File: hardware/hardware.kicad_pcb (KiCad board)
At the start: 2 copper layers, 19 parts, among them J1 Conn_01x02, J2 Conn_01x02, P1 USB_C_Plug, U2 ATmega328PB-A, U3 LM1117S-5, U4 CH340C, Y1 Crystal_GND24

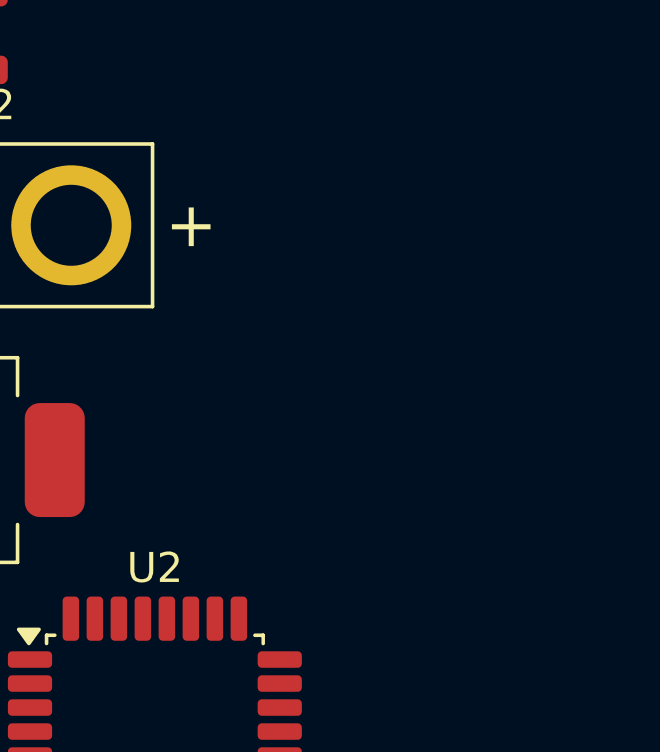
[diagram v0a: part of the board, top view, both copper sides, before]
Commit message: add isp connector
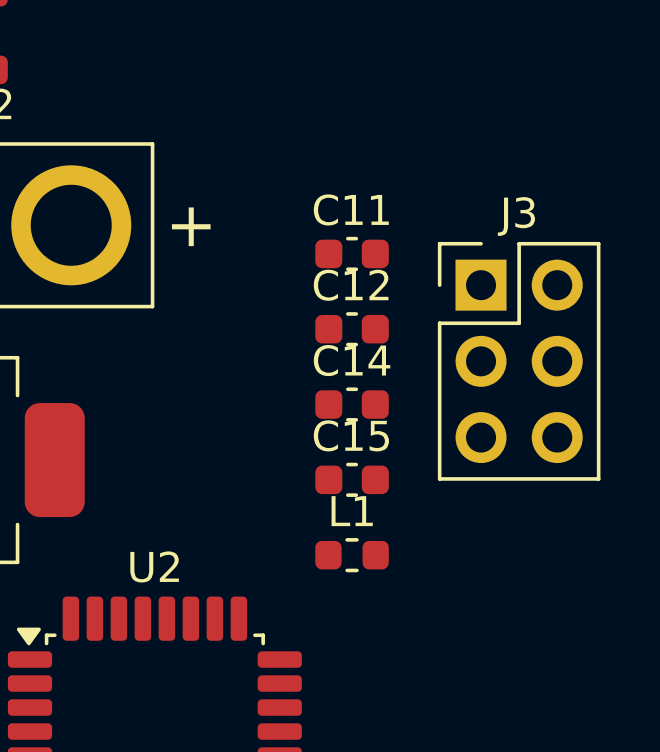
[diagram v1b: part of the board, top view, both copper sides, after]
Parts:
- added C11: 100n, Capacitor_SMD:C_0603_1608Metric, F.Cu at (134.9, 85.9)
- added C12: 100n, Capacitor_SMD:C_0603_1608Metric, F.Cu at (134.9, 88.4)
- added C14: 10n, Capacitor_SMD:C_0603_1608Metric, F.Cu at (134.9, 90.9)
- added C15: 1p, Capacitor_SMD:C_0603_1608Metric, F.Cu at (134.9, 93.4)
- added J3: AVR-ISP-6, Connector_PinHeader_2.54mm:PinHeader_2x03_P2.54mm_Vertical, F.Cu at (139.2, 86.9)
- added L1: L, Inductor_SMD:L_0603_1608Metric, F.Cu at (134.9, 95.9)
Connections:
- U2 pad 13: LED1 -> PWM1
- U2 pad 14: unconnected-(U2-PB2-Pad14) -> PWM2
- U2 pad 15: unconnected-(U2-PB3-Pad15) -> MOSI
- U2 pad 16: unconnected-(U2-PB4-Pad16) -> MISO
- U2 pad 17: unconnected-(U2-PB5-Pad17) -> SCK
- U2 pad 23: unconnected-(U2-PC0-Pad23) -> LED1
- U4 pad 14: unconnected-(U4-~{RTS}-Pad14) -> RST

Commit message: pcb wiring
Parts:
- added J4: Conn_01x03_Pin, Connector_PinHeader_2.54mm:PinHeader_1x03_P2.54mm_Vertical, F.Cu at (146.0, 85.3)
- added J5: Conn_01x03_Pin, Connector_PinHeader_2.54mm:PinHeader_1x03_P2.54mm_Vertical, F.Cu at (113.0, 86.2)
- added REF**: MountingHole_3.2mm_M3_DIN965_Pad, MountingHole:MountingHole_3.2mm_M3_DIN965_Pad, F.Cu at (119.0, 80.0)
- added REF**: MountingHole_3.2mm_M3_DIN965_Pad, MountingHole:MountingHole_3.2mm_M3_DIN965_Pad, F.Cu at (153.0, 88.0)
- added RV1: R_Potentiometer_Trim, Potentiometer_THT:Potentiometer_Runtron_RM-065_Vertical, F.Cu at (120.0, 87.8)
- added RV2: R_Potentiometer_Trim, Potentiometer_THT:Potentiometer_Runtron_RM-065_Vertical, F.Cu at (137.0, 87.8)
- moved C18 41.7 mm to (144.5, 68.0), turned to 180 degrees
- moved C19 35.8 mm to (135.5, 68.5), turned to -90 degrees
- moved J2 34.0 mm to (153.5, 76.5), turned to 90 degrees
- moved J1 30.9 mm to (140.3, 62.5)
- moved U3 29.9 mm to (130.0, 64.0), turned to 90 degrees
- moved C20 27.7 mm to (129.0, 71.5)
- moved C17 25.6 mm to (128.5, 69.5), turned to 180 degrees
- moved U2 25.6 mm to (135.0, 77.5)
- moved U4 25.3 mm to (122.0, 63.7)
- moved C8 21.9 mm to (127.2, 82.0), turned to 180 degrees
- moved C15 21.2 mm to (129.0, 73.0)
- moved C7 21.0 mm to (127.2, 76.0)
- moved L1 18.6 mm to (141.5, 78.5), turned to 90 degrees
- moved R1 16.8 mm to (111.0, 74.0), turned to 180 degrees
- moved C16 15.3 mm to (119.5, 72.0), turned to 180 degrees
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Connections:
- J1 pad 1: +BATT -> GND
- J1 pad 2: GND -> +BATT
- J2 pad 1: +BATT -> GND
- J2 pad 2: GND -> +BATT
- U2 pad 25: unconnected-(U2-PC2-Pad25) -> ADC2
- U2 pad 26: unconnected-(U2-PC3-Pad26) -> ADC1
- U2 pad 29: unconnected-(U2-~{RESET}/PC6-Pad29) -> RST
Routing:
- net VBUS: track 0.00 -> 129.4 mm
- net PWM1: track 0.00 -> 35.9 mm
- net +BATT: track 0.00 -> 31.3 mm
- net RST: track 0.00 -> 30.9 mm, vias 0 -> 2
- net LED1: track 0.00 -> 29.6 mm, vias 0 -> 2
- net ADC1: track 0.00 -> 25.8 mm, vias 0 -> 1
- net MOSI: track 0.00 -> 23.4 mm
- net ADC2: track 0.00 -> 21.6 mm, vias 0 -> 1
- net PWM2: track 0.00 -> 12.9 mm
- net SCK: track 0.00 -> 10.9 mm
- net MISO: track 0.00 -> 10.8 mm
- net XTAL1: track 0.00 -> 7.37 mm
- net GND: track 0.00 -> 6.43 mm, vias 0 -> 10
- net XTAL2: track 0.00 -> 5.03 mm
- net D+: track 0.00 -> 3.55 mm
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- added copper zone on B.Cu, net GND
- added copper zone on F.Cu, net GND
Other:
- board outline added: 49 x 37 mm
